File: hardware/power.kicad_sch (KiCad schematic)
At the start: 24 parts, among them IC1 LMR38020SQDDARQ1, IC2 LMR38020SQDDARQ1, U3 LM1117-3.3

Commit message: values-correction
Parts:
- C10, C11, C13, C14, C15, C16: value 100nF -> 100n
- C12: value 47uF -> 47u
- C17, C5, C9: value 10uF -> 10u
- L1: value 15uH -> 15u
- L2: value 22uH -> 22u
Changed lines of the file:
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@@
 			)
 		)
-		(property "Value" "100nF"
+		(property "Value" "100n"
 			(at 112.649 140.843 0)
 			(effects
@@
 			)
 		)
-		(property "Value" "100nF"
+		(property "Value" "100n"
 			(at 88.9 55.8862 0)
 			(effects
@@
 			)
 		)
-		(property "Value" "47uF"
+		(property "Value" "47u"
 			(at 200.66 53.3462 0)
 			(effects
@@
 			)
 		)
-		(property "Value" "10uF"
+		(property "Value" "10u"
 			(at 76.2 101.6062 0)
 			(effects
@@
 			)
 		)
-		(property "Value" "100nF"
+		(property "Value" "100n"
 			(at 88.9 101.6062 0)
 			(effects
@@
 			)
 		)
-		(property "Value" "10uF"
+		(property "Value" "10u"
 			(at 200.66 99.0662 0)
 			(effects
@@
 		(lib_id "Device:C_Small")
 		(at 157.48 88.9 90)
-		(mirror x)
 		(unit 1)
 		(exclude_from_sim no)
@@
 		(fields_autoplaced yes)
 		(property "Reference" "C16"
-			(at 157.4863 82.55 90)
-			(effects
-				(font
-					(size 1.27 1.27)
-				)
-			)
-		)
-		(property "Value" "100nF"
-			(at 157.4863 85.09 90)
+			(at 157.4863 95.25 90)
+			(effects
+				(font
+					(size 1.27 1.27)
+				)
+			)
+		)
+		(property "Value" "100n"
+			(at 157.4863 92.71 90)
 			(effects
 				(font
@@
 			)
 		)
-		(property "Value" "100nF"
+		(property "Value" "100n"
 			(at 148.971 140.843 0)
 			(effects
@@
 			)
 		)
-		(property "Value" "22uH"
+		(property "Value" "22u"
 			(at 172.72 83.82 90)
 			(effects
@@
 			)
 		)
-		(property "Value" "10uF"
+		(property "Value" "10u"
 			(at 76.2 55.8862 0)
 			(effects
@@
 		(lib_id "Device:C_Small")
 		(at 157.48 43.18 90)
-		(mirror x)
 		(unit 1)
 		(exclude_from_sim no)
@@
 		(fields_autoplaced yes)
 		(property "Reference" "C11"
-			(at 157.4863 36.83 90)
-			(effects
-				(font
-					(size 1.27 1.27)
-				)
-			)
-		)
-		(property "Value" "100nF"
-			(at 157.4863 39.37 90)
+			(at 157.4863 49.53 90)
+			(effects
+				(font
+					(size 1.27 1.27)
+				)
+			)
+		)
+		(property "Value" "100n"
+			(at 157.4863 46.99 90)
 			(effects
 				(font
@@
 			)
 		)
-		(property "Value" "15uH"
+		(property "Value" "15u"
 			(at 172.72 38.1 90)
 			(effects

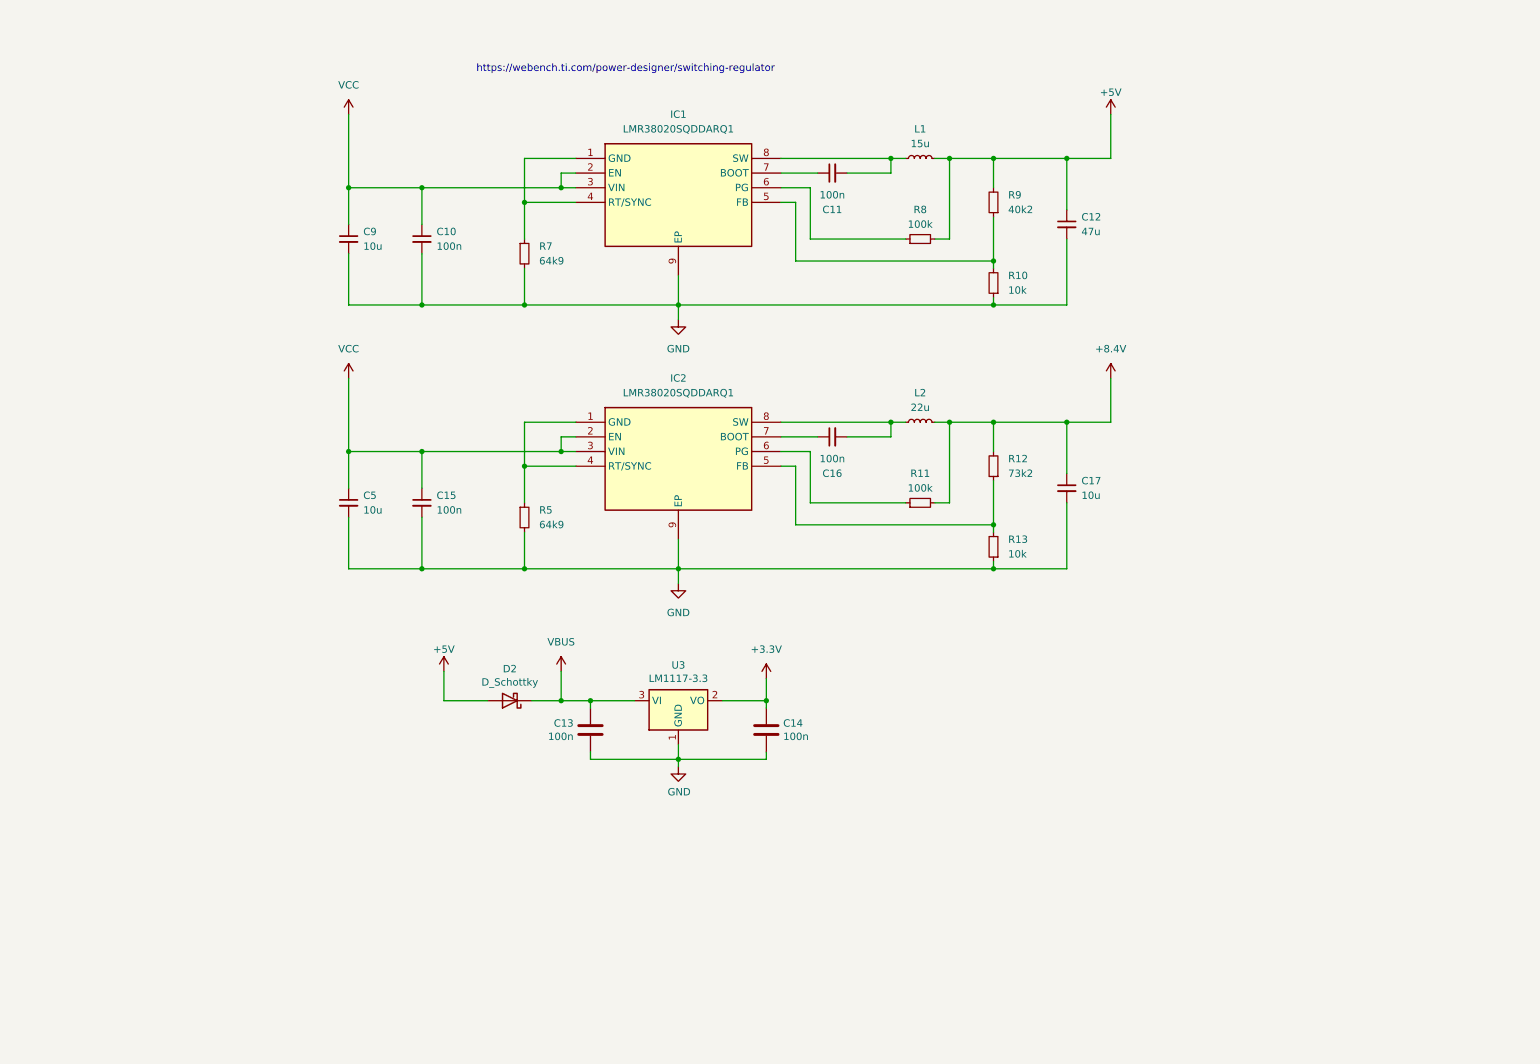
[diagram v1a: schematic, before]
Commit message: added sheet pins
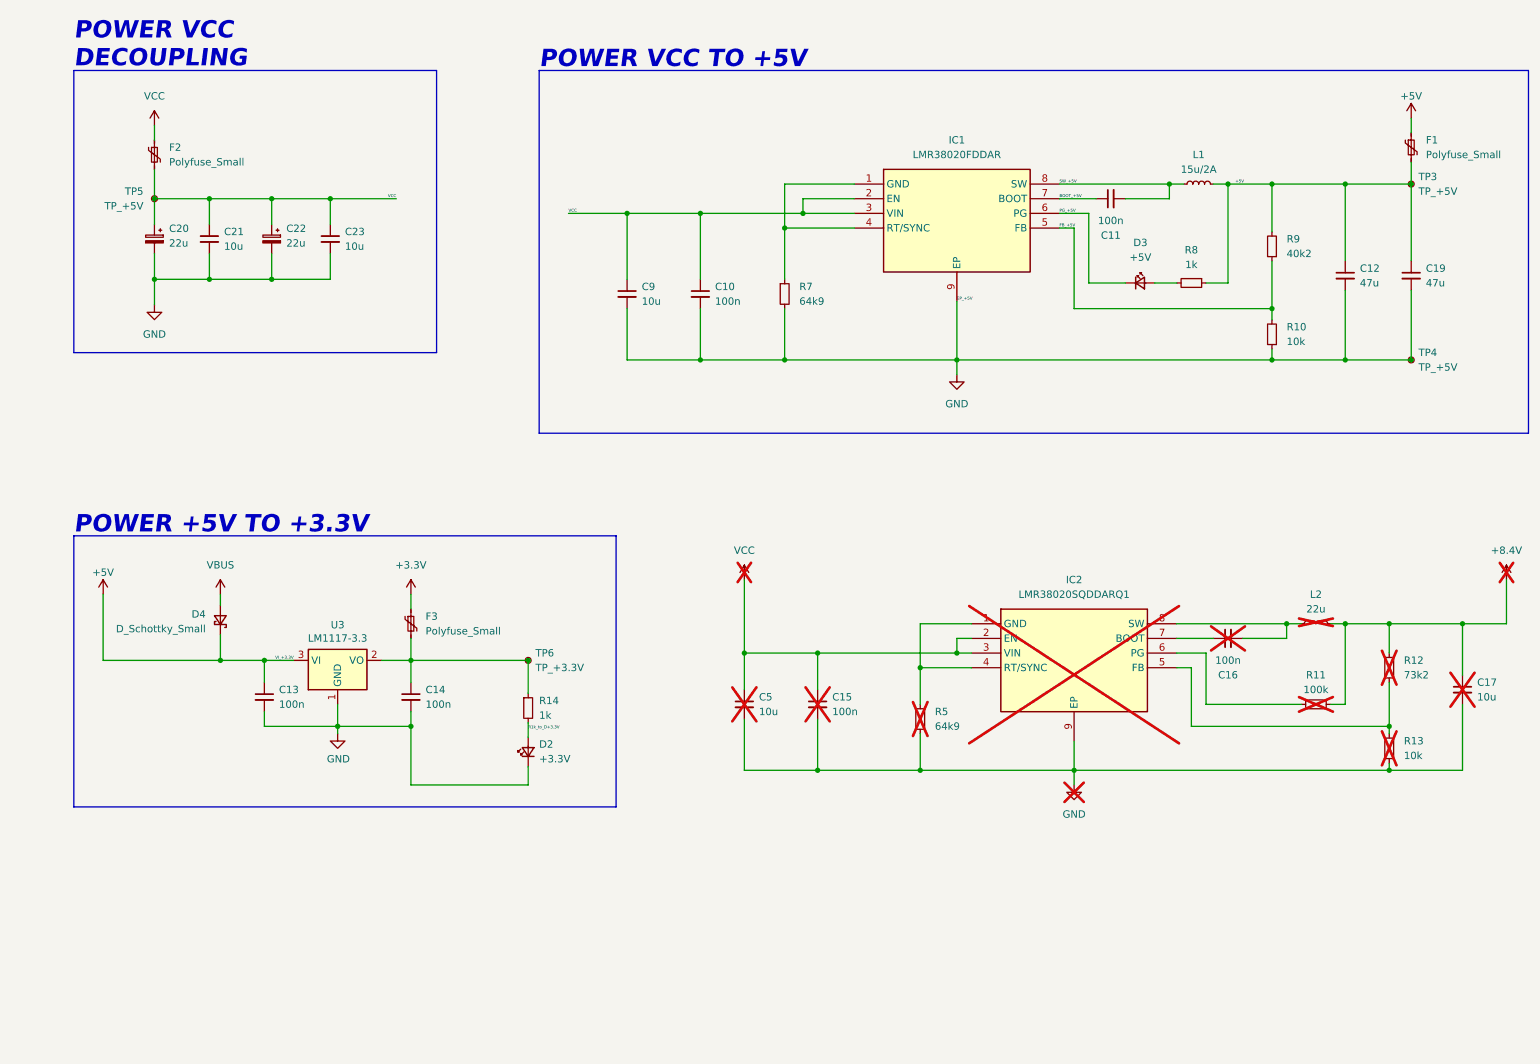
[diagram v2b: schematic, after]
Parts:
- removed C13, C14: 100n, Capacitor_SMD:C_0603_1608Metric_Pad1.08x0.95mm_HandSolder, symbol Device:C
- removed D2: D_Schottky, Diode_SMD:D_SOD-123, symbol Device:D_Schottky
- removed IC1: LMR38020SQDDARQ1, SOIC127P600X170-9N, symbol SamacSys_Parts:LMR38020SQDDARQ1
- added C13, C14: 100n, symbol Device:C_Small
- added C19: 47u, symbol Device:C_Small
- added C20, C22: 22u, Capacitor_SMD:CP_Elec_4x5.8, symbol Device:C_Polarized_Small
- added C21, C23: 10u, symbol Device:C_Small
- added D2: +3.3V, symbol Device:LED_Small
- added D3: +5V, symbol Device:LED_Small
- added D4: D_Schottky_Small, symbol Device:D_Schottky_Small
- added F1, F2, F3: Polyfuse_Small, symbol Device:Polyfuse_Small
- added IC1: LMR38020FDDAR, SOIC127P600X170-9N, symbol SamacSys_Parts:LMR38020FDDAR
- added R14: 1k, symbol Device:R_Small
- added TP3, TP4, TP5: TP_+5V, symbol Connector:TestPoint_Small
- added TP6: TP_+3.3V, symbol Connector:TestPoint_Small
- C15, C16, C17, C5, IC2, L2, R11, R12, R13, R5: now not fitted
- L1: value 15u -> 15u/2A
- R8: value 100k -> 1k
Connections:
- net +3.3V: now also F3.1; no longer U3.2 (VO)
- net +5V: now also R8.1, U3.3 (VI), C13.1, C19.1, D4.1 (K), F1.1, F1.2, TP3.1; no longer R8.2
- net GND: now also C13.2, C14.2, C19.2, C20.2, C21.2, C22.2, C23.2, D2.1 (K), IC1.9 (EP), TP4.1
- net VBUS: now also D4.2 (A); no longer U3.3 (VI)
- net VCC: now also C20.1, C21.1, C22.1, C23.1, F2.1, F2.2, IC1.2 (EN), IC1.3 (VIN), TP5.1
- net at R7.1: now also IC1.1 (GND), IC1.4 (RT/SYNC)
- net FB_+5V: now reaches R10.2, R9.1
- net FB_+5V: now also IC1.5 (FB)
- net BOOT_+5V: now reaches C11.1
- net BOOT_+5V: now also IC1.7 (BOOT)
- net SW_+5V: now reaches C11.2, L1.1
- net SW_+5V: now also IC1.8 (SW)
- new net: C14.1, F3.2, R14.1, TP6.1, U3.2 (VO)
- new net: D3.2 (A), R8.2
- new net PG_+5V: D3.1 (K), IC1.6 (PG)
- new net R1k_to_D+3.3V: D2.2 (A), R14.2
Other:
- note added: "POWER +5V TO +3.3V"
- note added: "POWER VCC DECOUPLING"
- note added: "POWER VCC TO +5V"
- note removed: "https://webench.ti.com/power-designer/switching-regulator"
- moved on the sheet: C10, C11, C12, C9, L1, R10, R7, R9, U3

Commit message: documentation update
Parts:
- removed C15, C16: 100n, symbol Device:C_Small
- removed C17, C5: 10u, symbol Device:C_Small
- removed IC2: LMR38020SQDDARQ1, SOIC127P600X170-9N, symbol SamacSys_Parts:LMR38020SQDDARQ1
- removed L2: 22u, symbol Device:L_Small
- removed R11: 100k, symbol Device:R_Small
- removed R12: 73k2, symbol Device:R_Small
- removed R13: 10k, symbol Device:R_Small
- removed R5: 64k9, symbol Device:R_Small
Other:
- moved on the sheet: C13, C14, D2, D4, F3, R14, TP6, U3

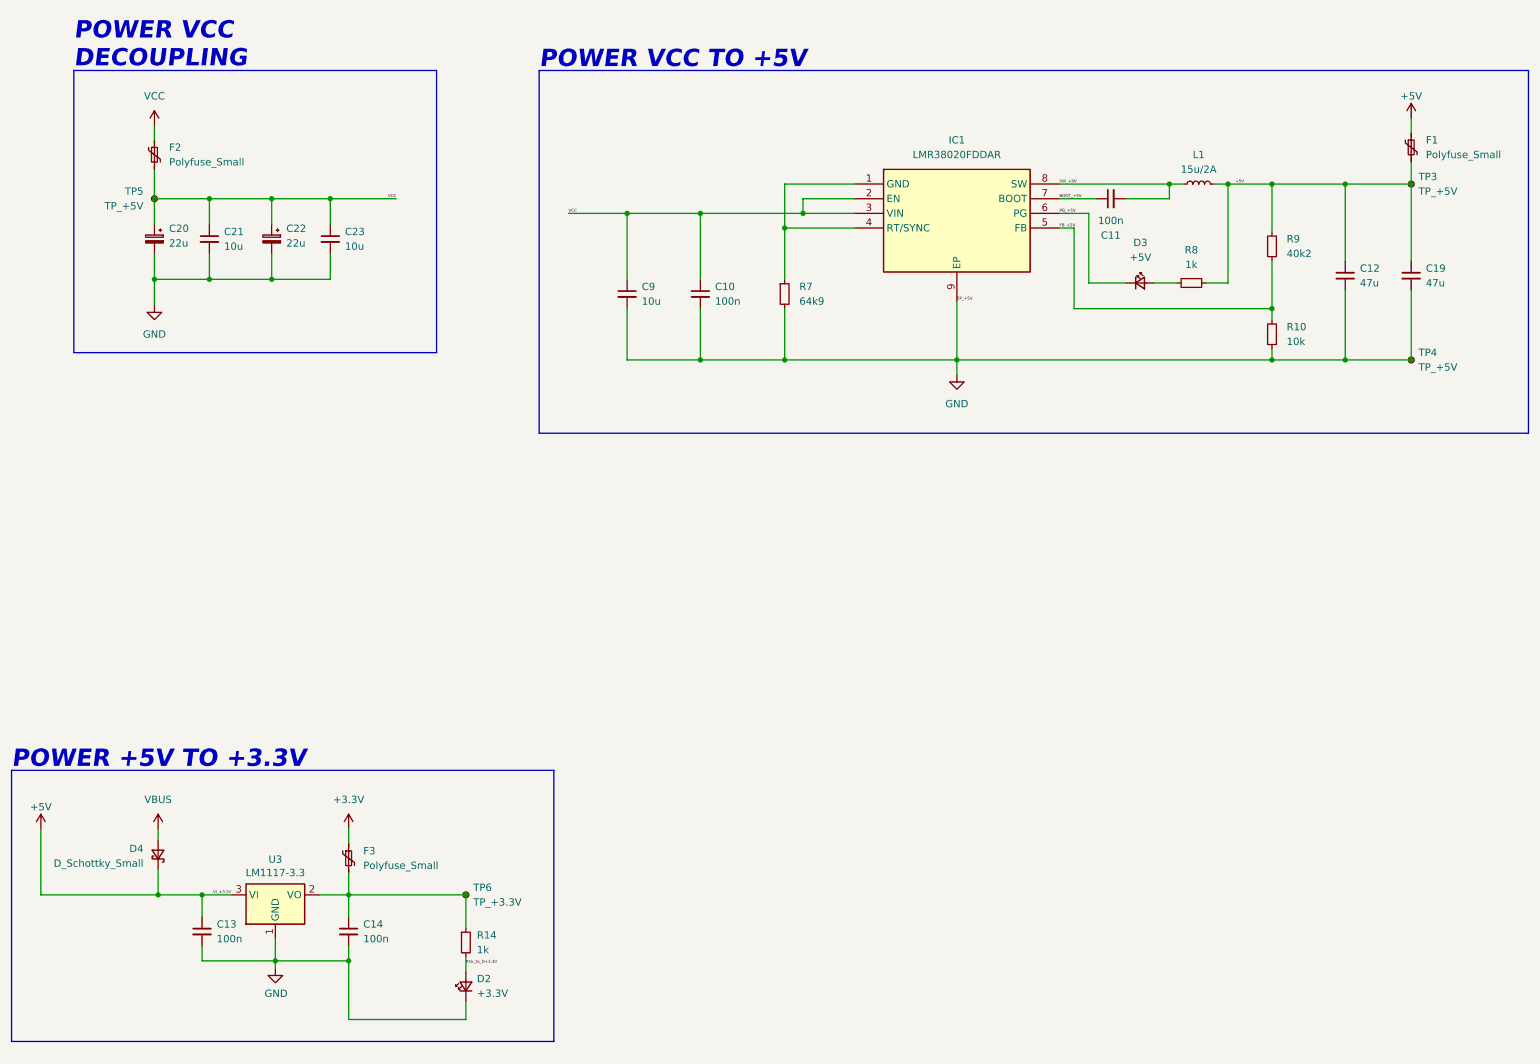
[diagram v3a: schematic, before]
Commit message: added 6V6 for servo
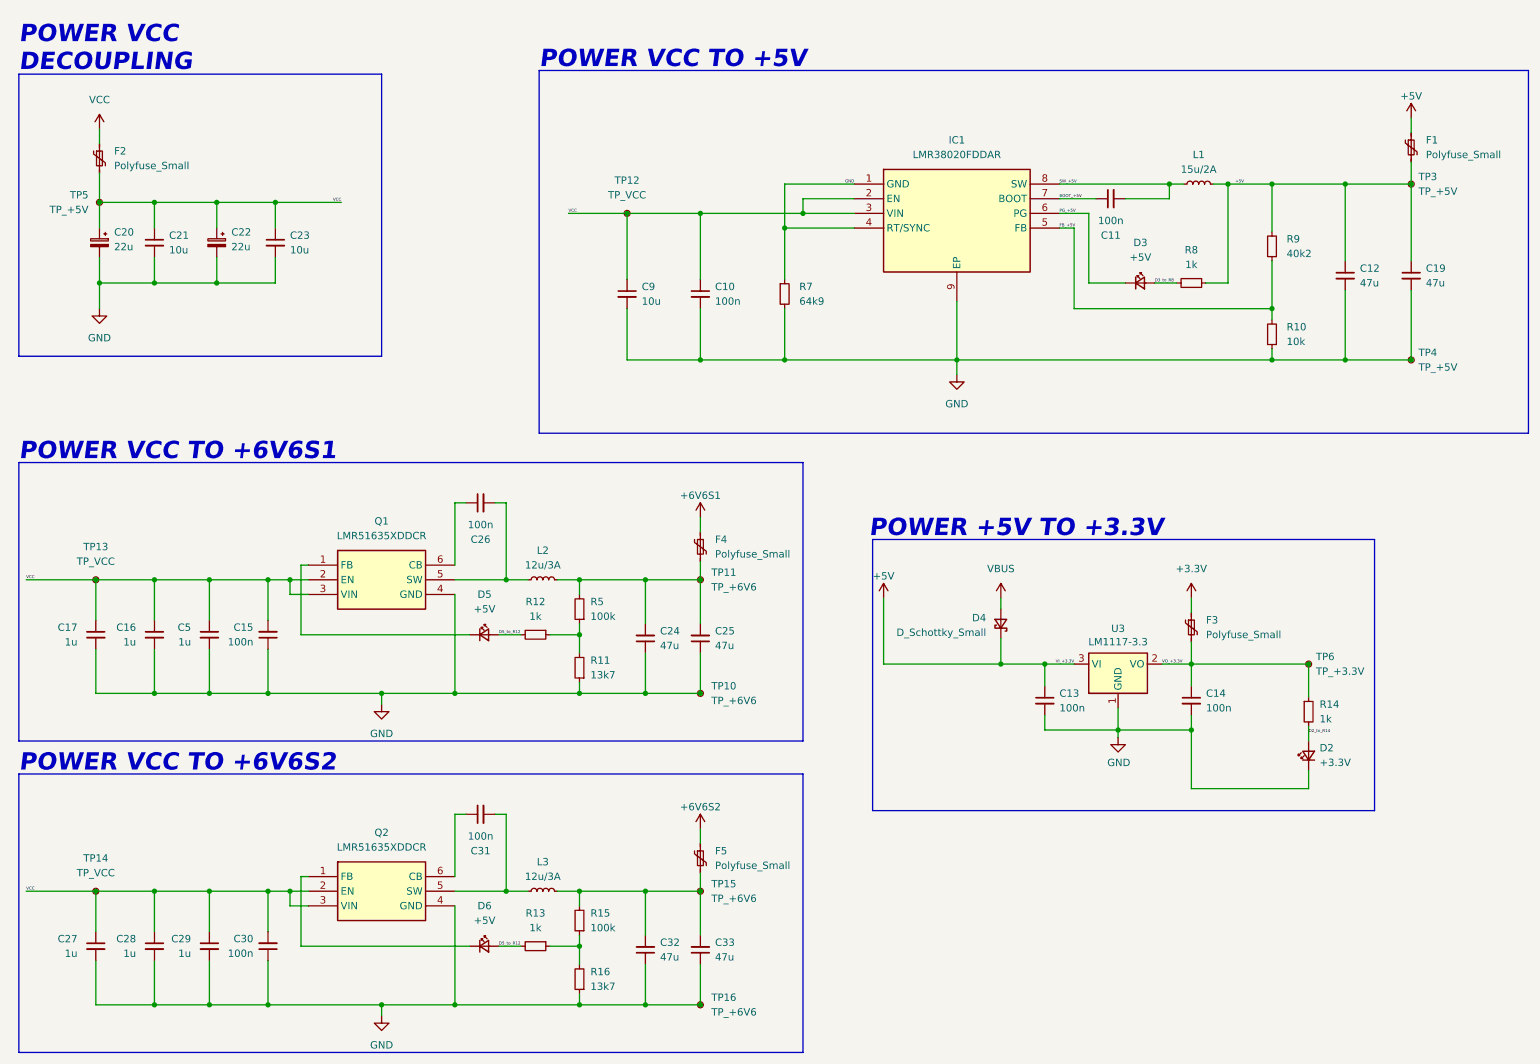
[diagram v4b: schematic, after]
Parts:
- added C15, C26, C30, C31: 100n, symbol Device:C_Small
- added C16, C17, C27, C28, C29, C5: 1u, symbol Device:C_Small
- added C24, C25, C32, C33: 47u, symbol Device:C_Small
- added D5, D6: +5V, symbol Device:LED_Small
- added F4, F5: Polyfuse_Small, symbol Device:Polyfuse_Small
- added L2, L3: 12u/3A, symbol Device:L_Small
- added Q1, Q2: LMR51635XDDCR, SOT95P280X110-6N, symbol SamacSys_Parts:LMR51635XDDCR
- added R11, R16: 13k7, symbol Device:R_Small
- added R12, R13: 1k, symbol Device:R_Small
- added R15, R5: 100k, symbol Device:R_Small
- added TP10, TP11, TP15, TP16: TP_+6V6, symbol Connector:TestPoint_Small
- added TP12, TP13, TP14: TP_VCC, symbol Connector:TestPoint_Small
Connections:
- net GND: now also IC1.1 (GND), IC1.4 (RT/SYNC), R7.1, C15.1, C16.2, C17.2, C24.1, C25.1, C27.2, C28.2, C29.2, C30.1, C32.1, C33.1, C5.2, Q1.4 (GND), Q2.4 (GND), R11.1, R16.1, TP10.1, TP16.1
- net VCC: now also C15.2, C16.1, C17.1, C27.1, C28.1, C29.1, C30.2, C5.1, Q1.2 (EN), Q1.3 (VIN), Q2.2 (EN), Q2.3 (VIN), TP12.1, TP13.1, TP14.1
- net VO_+3.3V: now reaches C14.1, F3.2, R14.1, TP6.1, U3.2 (VO)
- net D3_to_R8: now reaches D3.2 (A), R8.2
- net R1k_to_D+3.3V renamed D2_to_R14
- new net: D5.1 (K), Q1.1 (FB)
- new net: C24.2, C25.2, F4.2, L2.2, R5.2, TP11.1
- new net: C31.2, L3.1, Q2.5 (SW)
- new net: C32.2, C33.2, F5.2, L3.2, R15.2, TP15.1
- new net: R13.1, R15.1, R16.2
- new net: C26.1, Q1.6 (CB)
- new net: C26.2, L2.1, Q1.5 (SW)
- new net: D6.1 (K), Q2.1 (FB)
- new net: C31.1, Q2.6 (CB)
- new net: R11.2, R12.1, R5.1
- new net +6V6S1: F4.1
- new net +6V6S2: F5.1
- new net D5_to_R12: D5.2 (A), D6.2 (A), R12.2, R13.2
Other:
- note added: "POWER VCC TO +6V6S1"
- note added: "POWER VCC TO +6V6S2"
- moved on the sheet: C13, C14, C20, C21, C22, C23, D2, D4, F2, F3, R14, TP5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
